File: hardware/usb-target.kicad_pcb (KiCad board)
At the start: 2 copper layers, 37.6 x 12.1 mm, 14 parts, among them J1 USB_A, U1 ATtiny85V-10PU

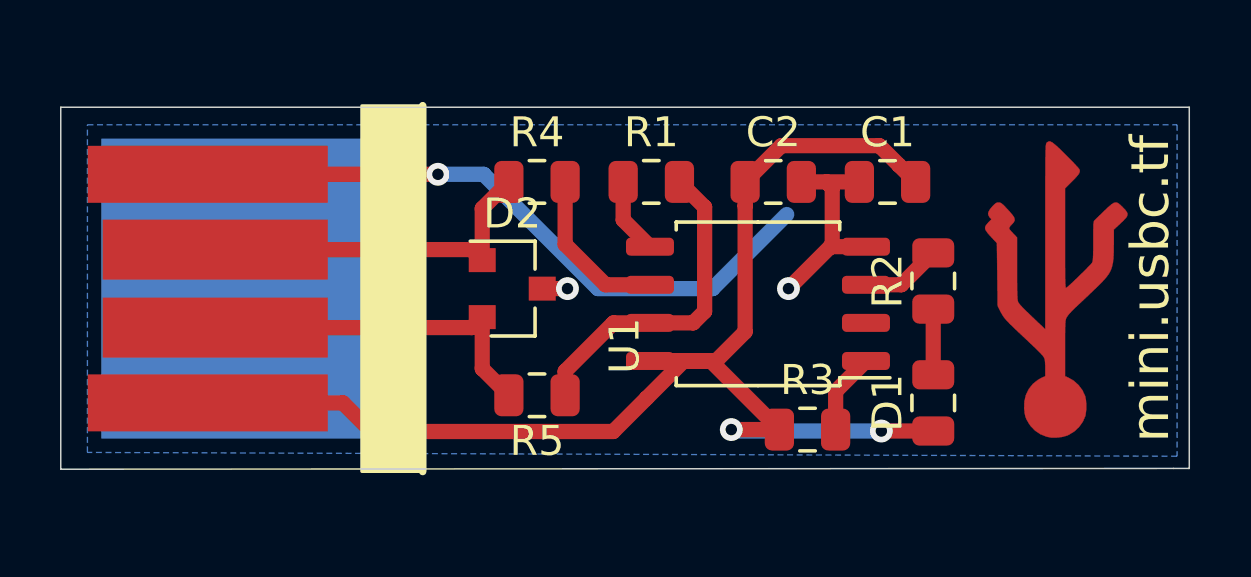
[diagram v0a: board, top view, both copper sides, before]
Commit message: hardware: update component value to match v-usb recommendations
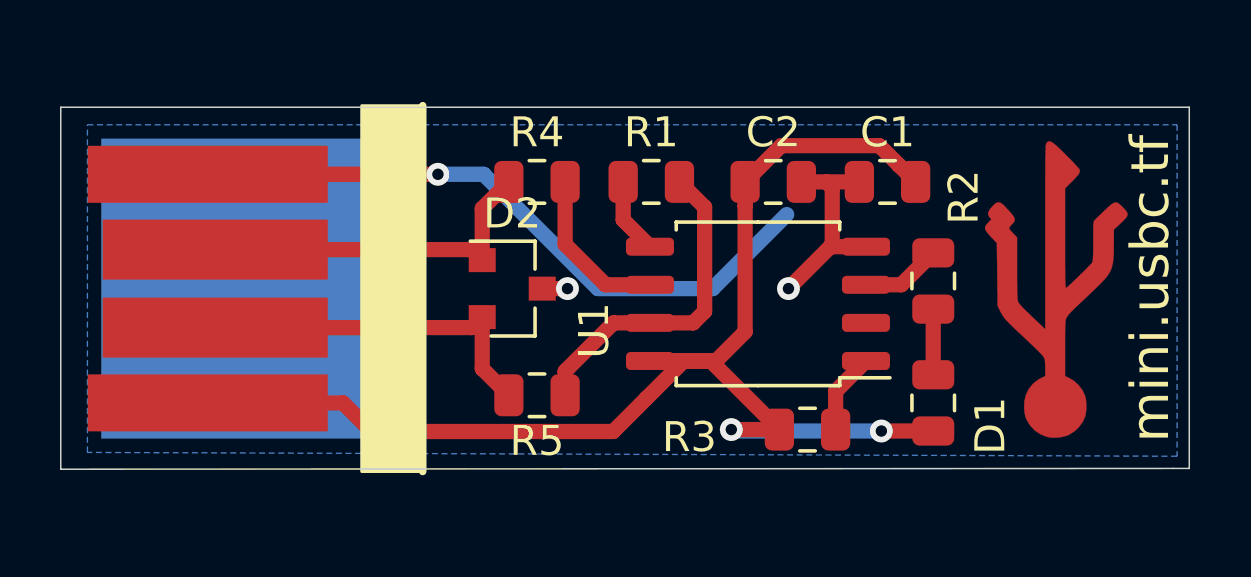
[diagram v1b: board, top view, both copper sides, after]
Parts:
- R1: value 1K -> 1.5K
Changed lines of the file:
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@@
   )
   (setup
-    (last_trace_width 0.508)
+    (last_trace_width 0.254)
     (user_trace_width 0.254)
     (user_trace_width 0.3048)
@@
     (tags "SOIC SO")
     (attr smd)
-    (fp_text reference U1 (at 4.445 -1.397 90) (layer F.SilkS)
+    (fp_text reference U1 (at 5.461 -0.889 90) (layer F.SilkS)
       (effects (font (size 1 1) (thickness 0.15)))
     )
@@
     (tags resistor)
     (attr smd)
-    (fp_text reference D1 (at 0 1.524 90) (layer F.SilkS)
+    (fp_text reference D1 (at 0.762 -1.905 90) (layer F.SilkS)
       (effects (font (size 1 1) (thickness 0.15)))
     )
@@
       (effects (font (size 1 1) (thickness 0.15)))
     )
-    (fp_text value 1K (at 0 1.65) (layer F.Fab)
+    (fp_text value 1.5K (at 0 1.65) (layer F.Fab)
       (effects (font (size 1 1) (thickness 0.15)))
     )
@@
     (tags resistor)
     (attr smd)
-    (fp_text reference R2 (at 0 -1.524 90) (layer F.SilkS)
+    (fp_text reference R2 (at 2.794 1.016 90) (layer F.SilkS)
       (effects (font (size 1 1) (thickness 0.15)))
     )
@@
     (tags resistor)
     (attr smd)
-    (fp_text reference R3 (at 0 -1.65) (layer F.SilkS)
-      (effects (font (size 1 1) (thickness 0.15)))
-    )
+    (fp_text reference R3 (at -3.937 0.254) (layer F.SilkS)
+      (effects (font (size 1 1) (thickness 0.15)))
+    )
